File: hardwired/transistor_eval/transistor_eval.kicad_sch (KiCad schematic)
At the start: 19 parts, among them Q1 NPN, Q2 NPN, Q3 NPN, Q4 NPN, Q5 NPN, U1 ${SIM.PARAMS}

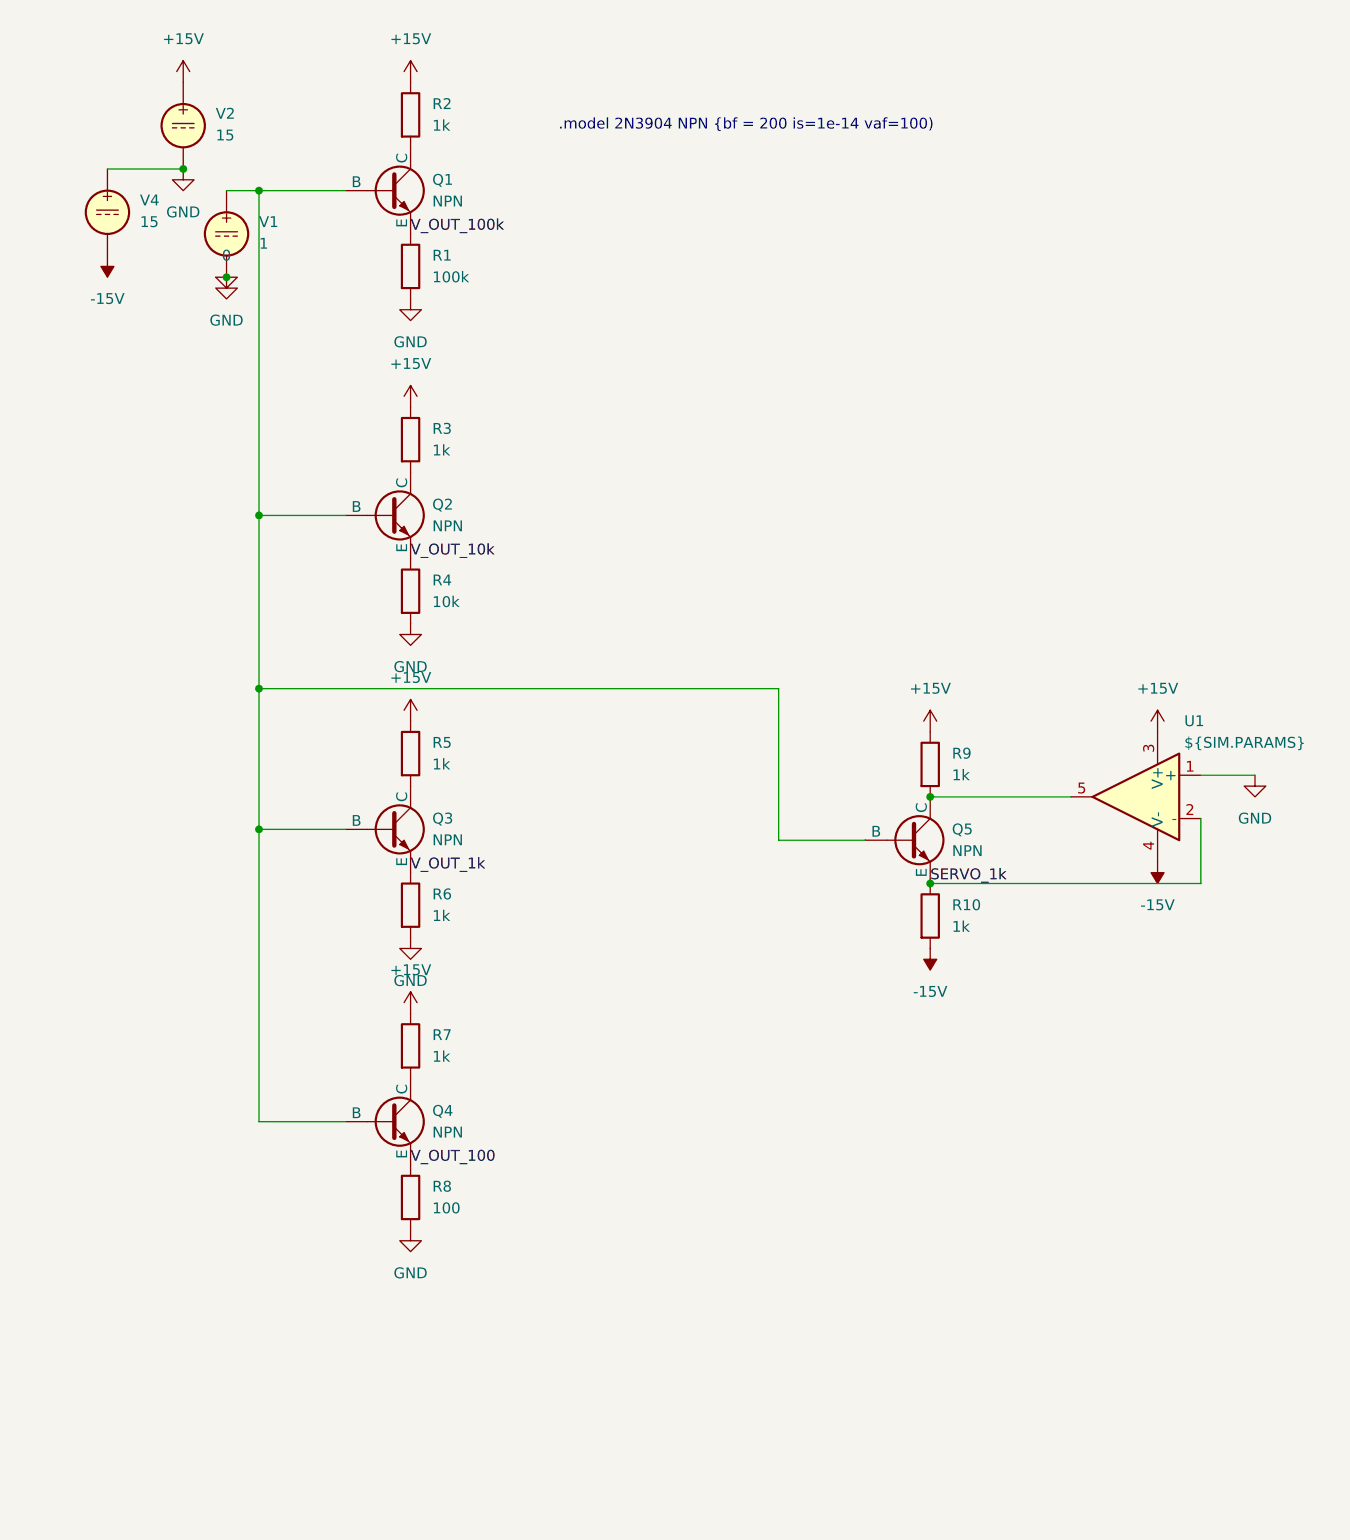
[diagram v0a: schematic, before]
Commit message: Add a simple SVG to match my breadboard
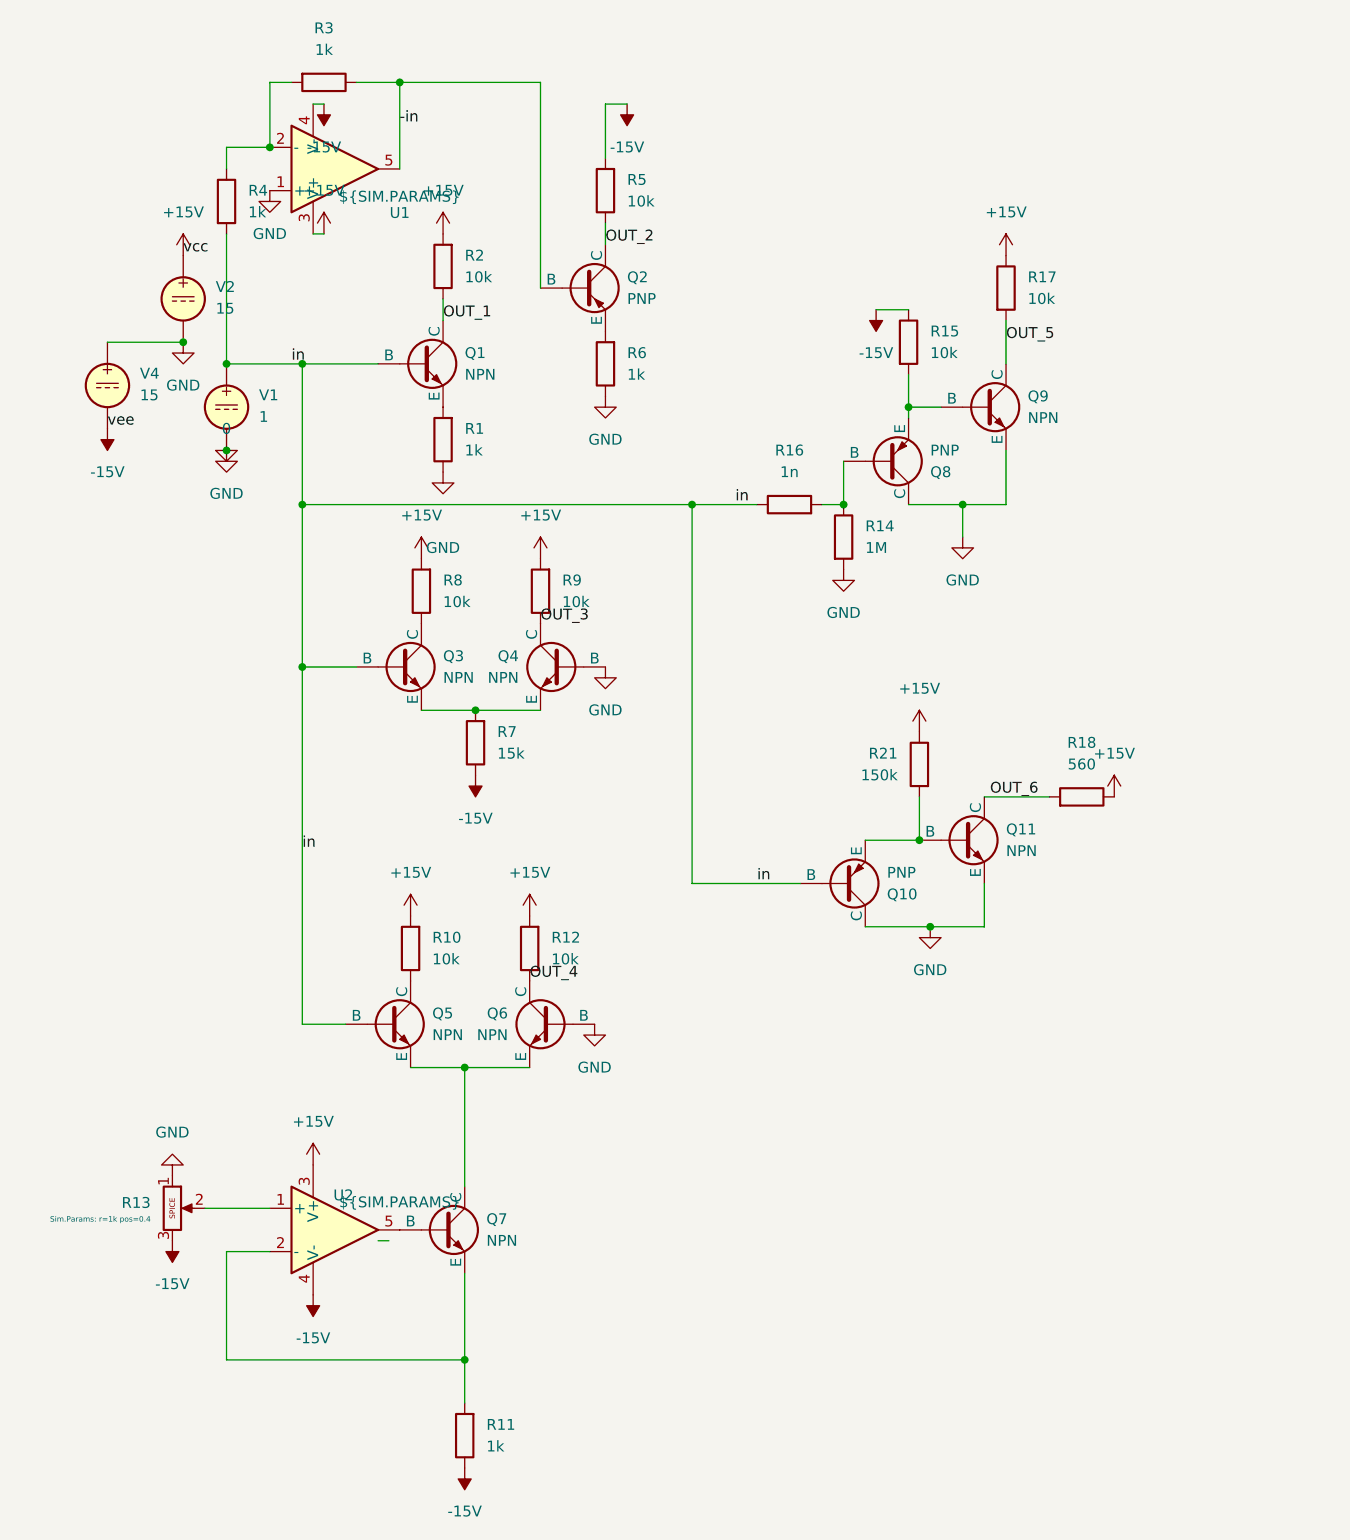
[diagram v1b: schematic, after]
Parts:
- removed Q2: NPN, symbol Simulation_SPICE:NPN
- added Q10, Q2, Q8: PNP, symbol Simulation_SPICE:PNP
- added Q11, Q6, Q7, Q9: NPN, symbol Simulation_SPICE:NPN
- added R11: 1k, symbol Device:R
- added R12, R15, R17: 10k, symbol Device:R
- added R13: Potentiometer, symbol Simulation_SPICE:Potentiometer
- added R14: 1M, symbol Device:R
- added R16: 1n, symbol Device:R
- added R18: 560, symbol Device:R
- added R21: 150k, symbol Device:R
- added U2: ${SIM.PARAMS}, symbol Simulation_SPICE:OPAMP
- R1: value 100k -> 1k
- R10, R2, R5, R9: value 1k -> 10k
- R4: value 10k -> 1k
- R7: value 1k -> 15k
- R8: value 100 -> 10k
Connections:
- net V_OUT_10k is gone; now on an unnamed net: R4.1
- net +15V: now also R10.2, R2.2, R8.2, R9.2, R12.2, R17.1, R18.1, R21.1, U2.3 (V+); no longer R2.1, R3.1, R5.1, R7.1, R9.1
- net -15V: now also R5.2, R7.1, R11.1, R13.3, R15.1, U2.4 (V-); no longer R10.2
- net 0: now also Q4.2 (B), R1.1, R6.1, Q10.1 (C), Q11.3 (E), Q6.2 (B), Q8.1 (C), Q9.3 (E), R13.1, R14.2; no longer R1.2, R4.2, R6.2, R8.2
- net at R3.2: now also U1.2 (-)
- net in: now reaches Q1.2 (B), Q3.2 (B), Q5.2 (B), V1.1
- net in: now also R4.2, Q10.2 (B), R16.1; no longer Q4.2 (B)
- net OUT_1: now reaches Q1.1 (C)
- net OUT_1: now also R2.1; no longer R2.2
- net at Q3.1 (C): now also R8.1; no longer R5.2
- net at R7.2: now also Q3.3 (E), Q4.3 (E); no longer Q4.1 (C)
- removed net SERVO_1k: Q5.3 (E), R10.1, U1.2 (-)
- removed net V_OUT_100: Q4.3 (E), R8.1
- net V_OUT_100k: no longer names the net of Q1.3 (E)
- net V_OUT_100k: now also R1.2; no longer R1.1
- removed net V_OUT_1k: Q3.3 (E), R6.1
- new net: R13.2, U2.1 (+)
- new net: Q7.3 (E), R11.2, U2.2 (-)
- new net: Q7.2 (B), U2.5
- new net: Q8.3 (E), Q9.2 (B), R15.2
- new net: Q5.1 (C), R10.1
- new net: Q5.3 (E), Q6.3 (E), Q7.1 (C)
- new net: Q10.3 (E), Q11.2 (B), R21.2
- new net: Q8.2 (B), R14.1, R16.2
- new net: Q2.3 (E), R6.2
- new net -in: Q2.2 (B), R3.1, U1.5
- new net OUT_2: Q2.1 (C), R5.1
- new net OUT_3: Q4.1 (C), R9.1
- new net OUT_4: Q6.1 (C), R12.1
- new net OUT_5: Q9.1 (C), R17.2
- new net OUT_6: Q11.1 (C), R18.2
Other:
- note removed: ".model 2N3904 NPN {bf = 200 is=1e-14 vaf=100)"
- moved on the sheet: V1, V2, V4
